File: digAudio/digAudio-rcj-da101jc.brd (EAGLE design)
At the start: 18.8 x 19.7 mm, 12 parts, among them IC1 DIT4096-H

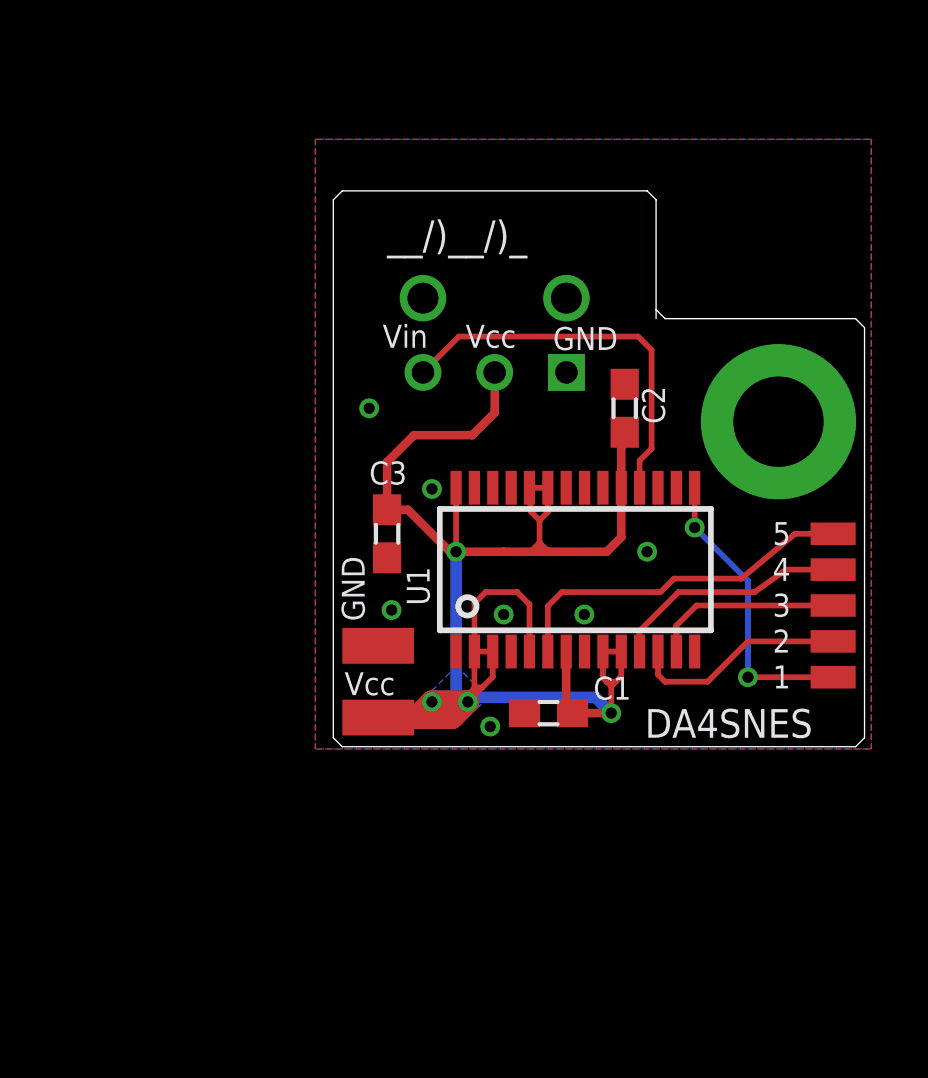
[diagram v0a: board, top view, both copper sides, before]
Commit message: update digital audio mod incl a new no-cut design with coax
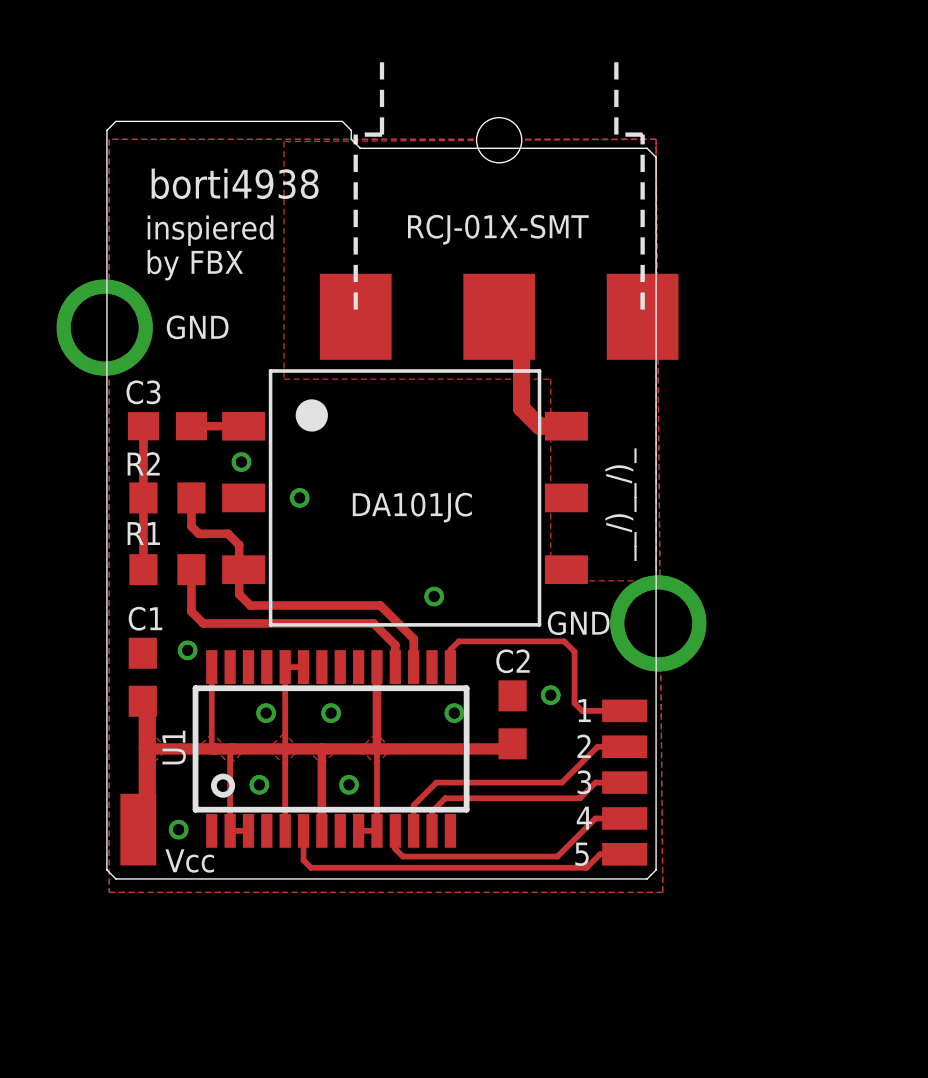
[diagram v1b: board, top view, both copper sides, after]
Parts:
- removed GND: (no value), wirepad:SMD1,27-2,54
- added R1: 360, rcl:R0603
- added R2: 91, rcl:R0603
- added U$2: DA10XJC, cs8406:DA101JC
- C3: value 0.1uF -> 10nF
- U$1: value PLT133/T10W -> RCJ-013-SMT-TR; device cs8406:PLT133/T10W -> digAudio_SNES:RCJ_01X_SMT_MODIFIED
- moved C1 14.4 mm to (-6.11, 2.54), turned to 90 degrees
- moved 5 13.5 mm to (11.0, -3.73)
- moved C2 11.7 mm to (6.99, 1.03)
- moved 4 11.5 mm to (11.0, -2.46)
- moved IC1 10.7 mm to (0.56, 0.00)
- moved 3 9.69 mm to (11.0, -1.19)
- moved VCC 9.37 mm to (-6.27, -2.86), turned to 180 degrees
- moved C3 8.66 mm to (-5.24, 11.4), turned to 0 degrees
- moved 2 8.27 mm to (11.0, 0.08)
- moved 1 7.48 mm to (11.0, 1.35)
- moved U$1 2.23 mm to (6.51, 15.6), flipped to the top, turned to 270 degrees
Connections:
- new net N$10: U$1.1A, U$1.1B, U$2.4
- new net N$11: C3.2, U$2.1
- new net N$7: IC1.17, R2.1, U$2.3
- new net N$8: C3.1, R1.2, R2.2
- new net N$9: U$1.2, U$2.6
- net GND: now also U$2.2; no longer C3.2, GND.1, U$1.P$1
- net N$1: now also R1.1; no longer U$1.P$3
- net VCC: no longer C3.1, U$1.P$2
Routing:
- net VCC: track 66.8 -> 40.4 mm, vias 4 -> 0
- net N$7: track 0.00 -> 12.7 mm
- net N$9: track 0.00 -> 5.84 mm
- net N$8: track 0.00 -> 5.08 mm
- net N$1: track 13.9 -> 9.97 mm
- net N$11: track 0.00 -> 1.85 mm
- net N$3: track 7.72 -> 9.24 mm
- net N$2: track 10.5 -> 9.00 mm, vias 2 -> 0
- net N$5: track 6.77 -> 7.93 mm
- net N$4: track 8.41 -> 9.44 mm
- added copper zone on layer 1, net N$10
- added copper zone on layer 1, net VCC
- removed copper zone on layer 16, net VCC
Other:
- board size 18.8 x 19.7 mm -> 19.4 x 26.8 mm
- board text added: "DA101JC"
- board text added: "Digital Audio for SNES RCA-output version"
- board text added: "R1"
- board text added: "R2"
- board text added: "RCJ-01X-SMT"
- board text added: "borti4938"
- board text added: "inspiered by FBX"
- board text removed: "DA4SNES"
- board text removed: "Vin"

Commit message: PCB Update
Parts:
- added GND: (no value), wirepad:1,6/0,9
- added J1: (no value), jumper:SJ_2
- C3: value 10nF -> 10nF/0.1uuF
- R1: value 360 -> 347.5/57
- R2: value 91 -> 90.9/open
- VCC: device wirepad:SMD1,27-2,54 -> wirepad:1,6/0,9
- moved VCC 12.7 mm to (5.00, -8.81), turned to 0 degrees
- moved R2 3.18 mm to (-5.08, 12.1)
- moved C3 3.04 mm to (-3.57, 14.0)
- moved R1 0.96 mm to (-6.11, 6.75), turned to 90 degrees
- moved U$2 0.64 mm to (3.81, 8.89)
- moved C1 0.64 mm to (-6.11, 1.91)
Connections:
- new net N$12: J1.2, R2.1, U$2.3
- net GND: now also GND.1, J1.1
- net N$7: now also J1.3; no longer R2.1, U$2.3
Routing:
- net VCC: track 40.4 -> 56.9 mm
- net N$12: track 0.00 -> 8.83 mm
- net N$11: track 1.85 -> 5.01 mm
- net N$8: track 5.08 -> 8.20 mm
- net N$7: track 12.7 -> 10.1 mm
- net N$1: track 9.97 -> 11.1 mm
- net N$9: track 5.84 -> 6.47 mm
- net GND: track 0.00 -> 0.56 mm, vias 13 -> 14
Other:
- board size 19.4 x 26.8 mm -> 19.4 x 31 mm
- board text added: "DA4SNES"
- board text added: "J1"
- board text added: "Tx+"
- board text added: "Tx-"
- board text added: "inspired by FBX"
- board text removed: "inspiered by FBX"
